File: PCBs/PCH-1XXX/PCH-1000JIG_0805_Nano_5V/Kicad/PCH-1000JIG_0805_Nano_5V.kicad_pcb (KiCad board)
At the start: 2 copper layers, 14.8 x 11 mm, 13 parts

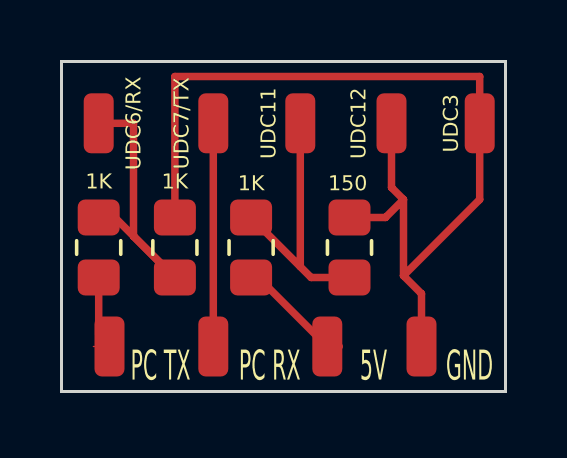
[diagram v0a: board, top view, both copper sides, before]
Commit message: Changed wrong resistor value
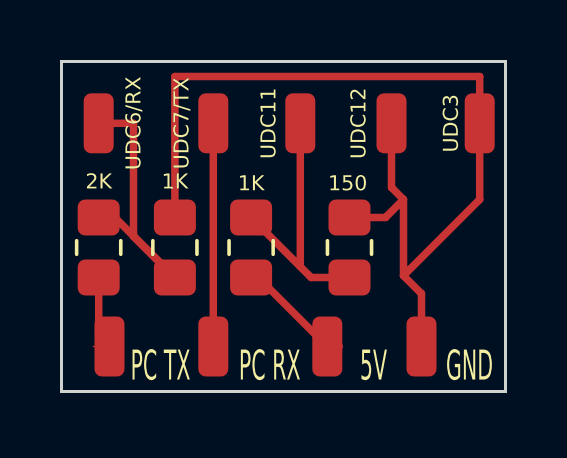
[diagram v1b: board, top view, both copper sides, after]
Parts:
- renumbered 1K to 2K
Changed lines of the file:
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@@
     (tags "resistor handsolder")
     (attr smd)
-    (fp_text reference "1K" (at 2.2 -2.54) (layer "F.SilkS")
+    (fp_text reference "2K" (at 2.2 -2.54) (layer "F.SilkS")
         (effects (font (size 0.5 0.5) (thickness 0.15)))
     )
